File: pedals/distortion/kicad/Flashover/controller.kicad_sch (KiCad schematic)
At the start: 24 parts, among them J4 SWD, U4 RP2040, U5 W25Q16JVSS, U6 AP2112K-3.3, Y1 12MHz

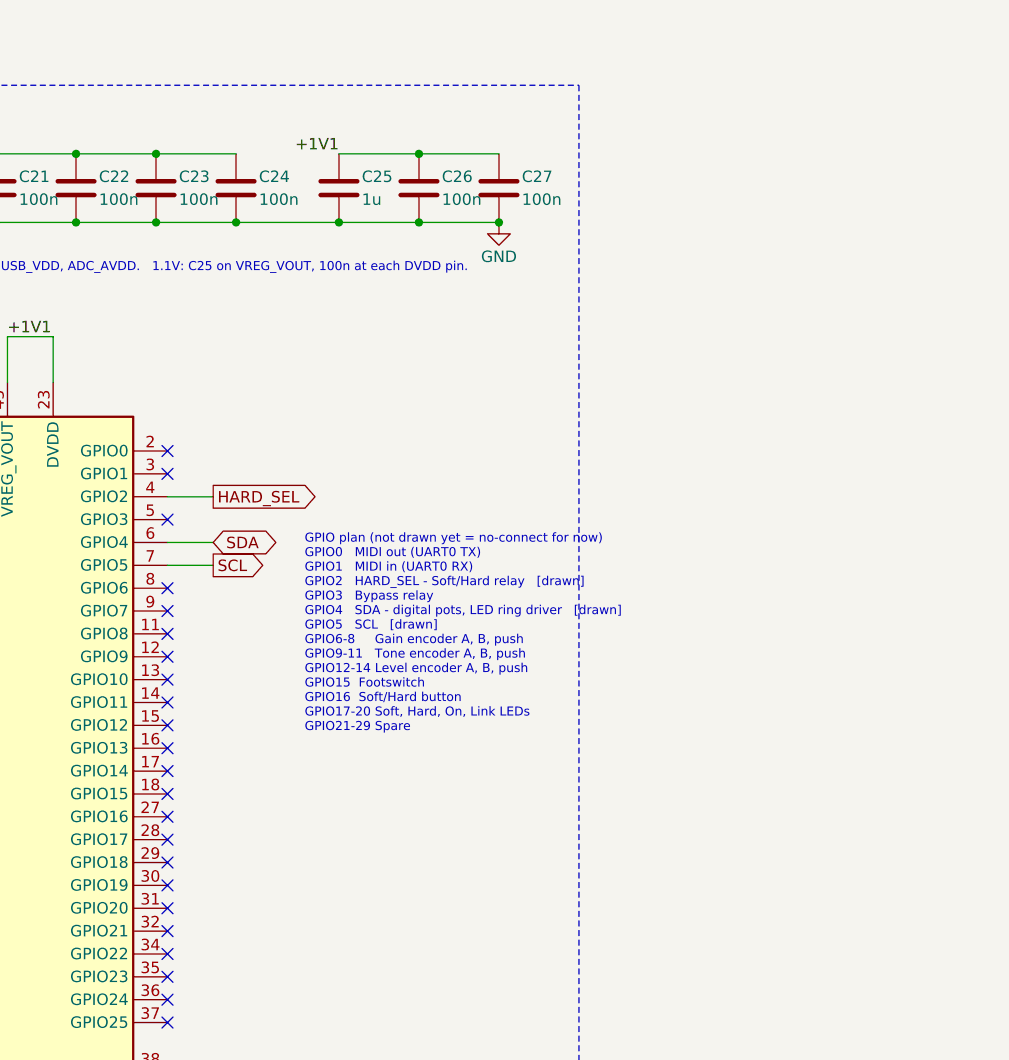
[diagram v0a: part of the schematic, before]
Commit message: Add Flashover controls and LED ring sheets
Controls sheet: three PEC11R encoders with push switches (pull-ups and
RC filtering) and the Soft/Hard button. LED Rings sheet: IS31FL3236A
driving three 11-LED rings plus Soft, Hard and On LEDs, on its own I2C
bus. Controller sheet wires the new GPIOs; the 5V regulator becomes an
L7805 for the LED load. ERC clean.

Co-Authored-By: Claude Opus 5.5 <noreply@anthropic.com>
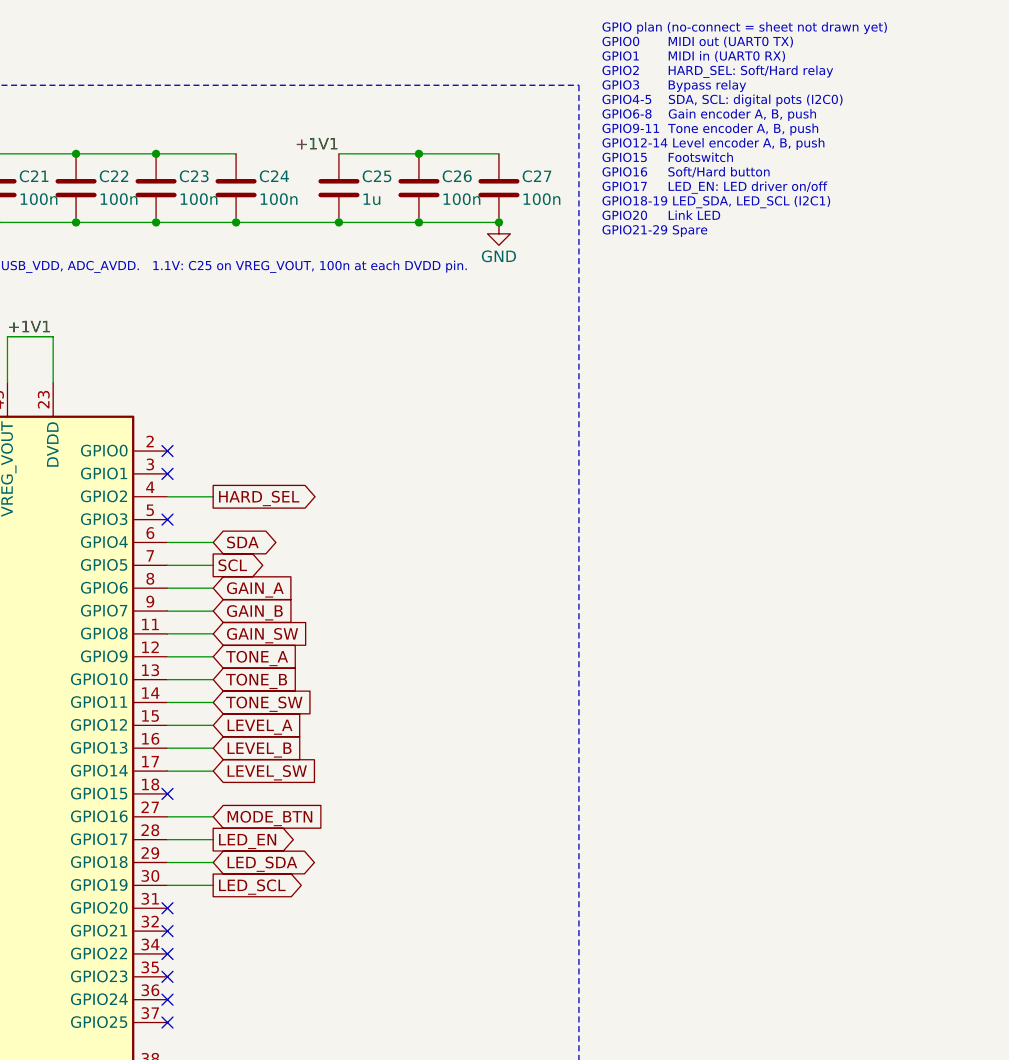
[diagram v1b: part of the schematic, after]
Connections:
- net GAIN_SW: now reaches U4.11 (GPIO8)
- net TONE_A: now reaches U4.12 (GPIO9)
- net TONE_B: now reaches U4.13 (GPIO10)
- net TONE_SW: now reaches U4.14 (GPIO11)
- net LEVEL_A: now reaches U4.15 (GPIO12)
- net LEVEL_B: now reaches U4.16 (GPIO13)
- net LEVEL_SW: now reaches U4.17 (GPIO14)
- net MODE_BTN: now reaches U4.27 (GPIO16)
- net LED_EN: now reaches U4.28 (GPIO17)
- net LED_SDA: now reaches U4.29 (GPIO18)
- net LED_SCL: now reaches U4.30 (GPIO19)
- net GAIN_A: now reaches U4.8 (GPIO6)
- net GAIN_B: now reaches U4.9 (GPIO7)
- no-connect marks 30 -> 17
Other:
- note added: "GPIO plan (no-connect = sheet not drawn yet) GPIO0 MIDI out (UART0 TX) GPIO1 MIDI in (UART0 RX) GPIO2 HARD_SEL: Soft/Hard relay GPIO3 Bypass relay GPIO4-5 SDA, SCL: digital pots (I2C0) GPIO6-8 Gain encoder A, B, push GPIO9-11 Tone encoder A, B, push GPIO12-14 Level encoder A, B, push GPIO15 Footswitch GPIO16 Soft/Hard button GPIO17 LED_EN: LED driver on/off GPIO18-19 LED_SDA, LED_SCL (I2C1) GPIO2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"
- note removed: "GPIO plan (not drawn yet = no-connect for now) GPIO0 MIDI out (UART0 TX) GPIO1 MIDI in (UART0 RX) GPIO2 HARD_SEL - Soft/Hard relay [drawn] GPIO3 Bypass relay GPIO4 SDA - digital pots, LED ring driver [drawn] GPIO5 SCL [drawn] GPIO6-8 Gain encoder A, B, push GPIO9-11 Tone encoder A, B, push GPIO12-14 Level encoder A, B, push GPIO15 Footswitch GPIO16 Soft/Hard button GPIO17-20 Soft, Hard, On, Link 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"

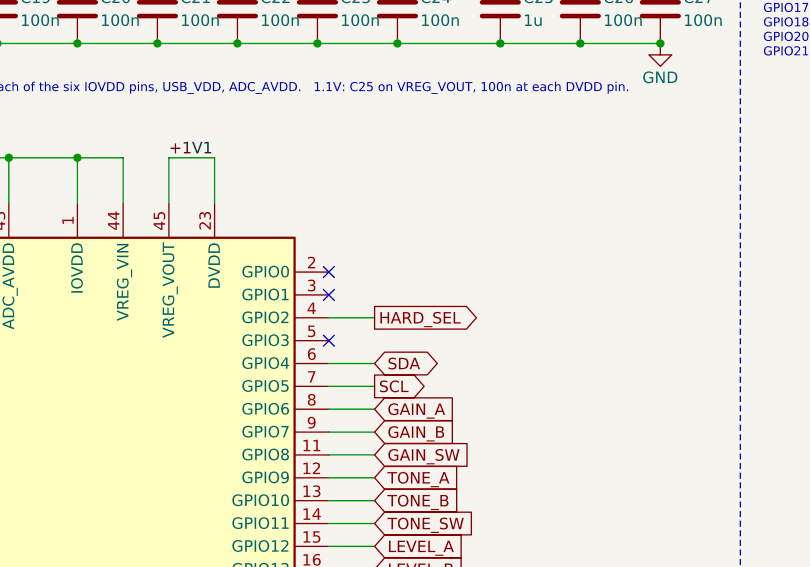
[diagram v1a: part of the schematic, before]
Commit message: Add Flashover MIDI sheet
MIDI in (H11L1 optocoupler, 220 ohm, reverse-protection diode, sleeve
unconnected) and MIDI out (3.3V drive: 33 ohm to pin 4, 10 ohm to pin 5)
on 3.5 mm TRS Type A jacks, wired to UART0. Root sheet re-spaced for
nine sheets. ERC clean.

Co-Authored-By: Claude Opus 5.5 <noreply@anthropic.com>
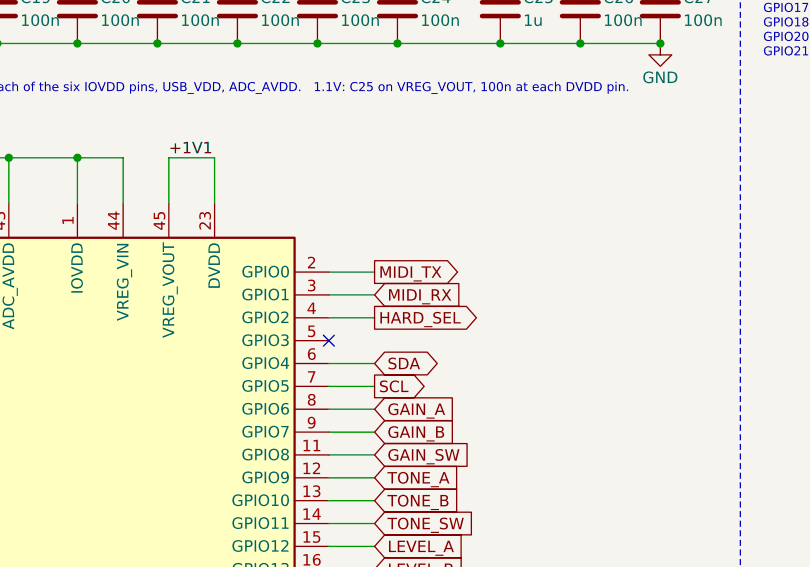
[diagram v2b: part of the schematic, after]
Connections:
- net MIDI_TX: now reaches U4.2 (GPIO0)
- net MIDI_RX: now reaches U4.3 (GPIO1)
- no-connect marks 17 -> 15

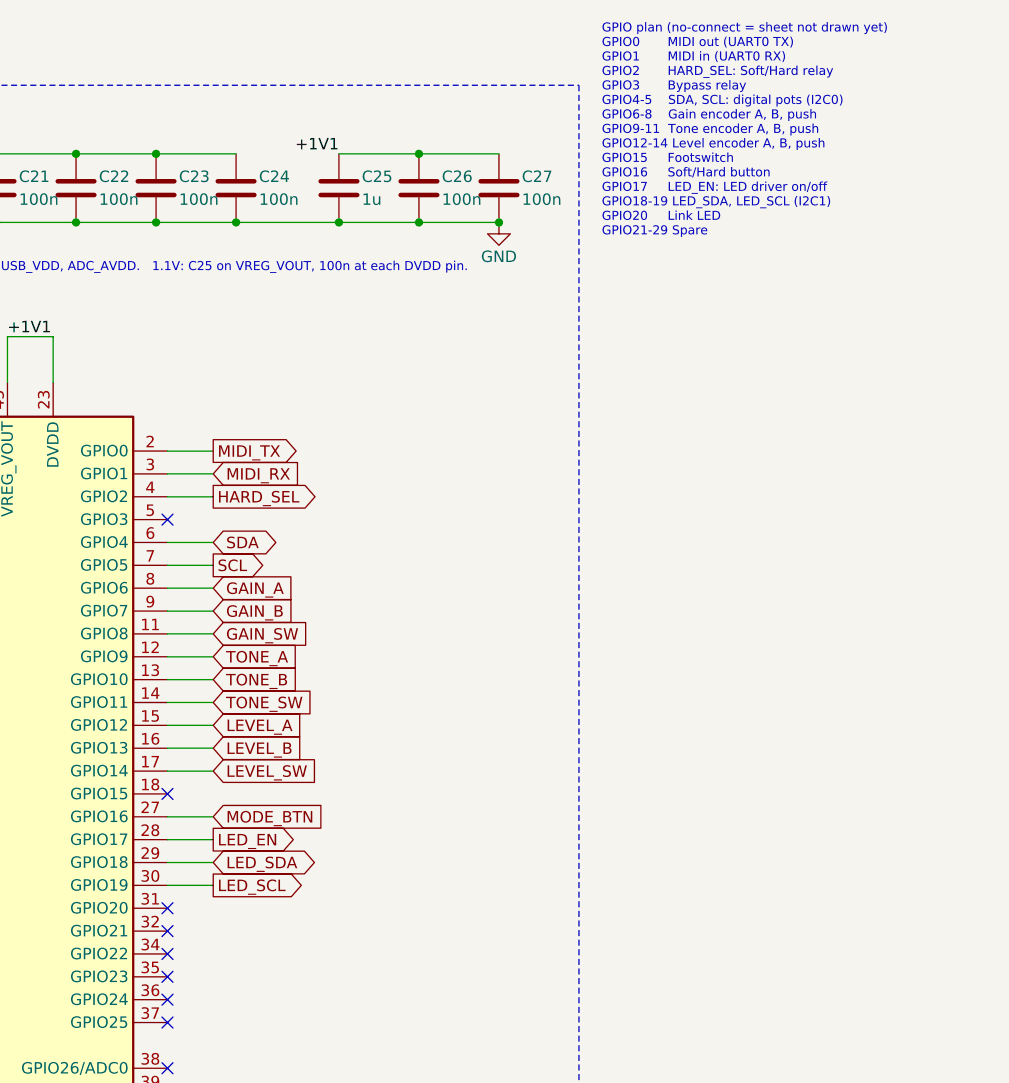
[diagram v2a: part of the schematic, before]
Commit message: Add Flashover bypass sheet; complete schematic
Bypass sheet: fail-safe G6K-2 relay bypass (NC contacts join the jacks
when unpowered), input/output jacks moved here from the audio sheets
(now FX_IN/FX_OUT), relay driver on FX_ON, soft-touch footswitch and
Link LED. Relay coils on K1 and K2 now take +5V on pin 1 (marked +).
Root sheet laid out in four columns. ERC clean.

Co-Authored-By: Claude Opus 5.5 <noreply@anthropic.com>
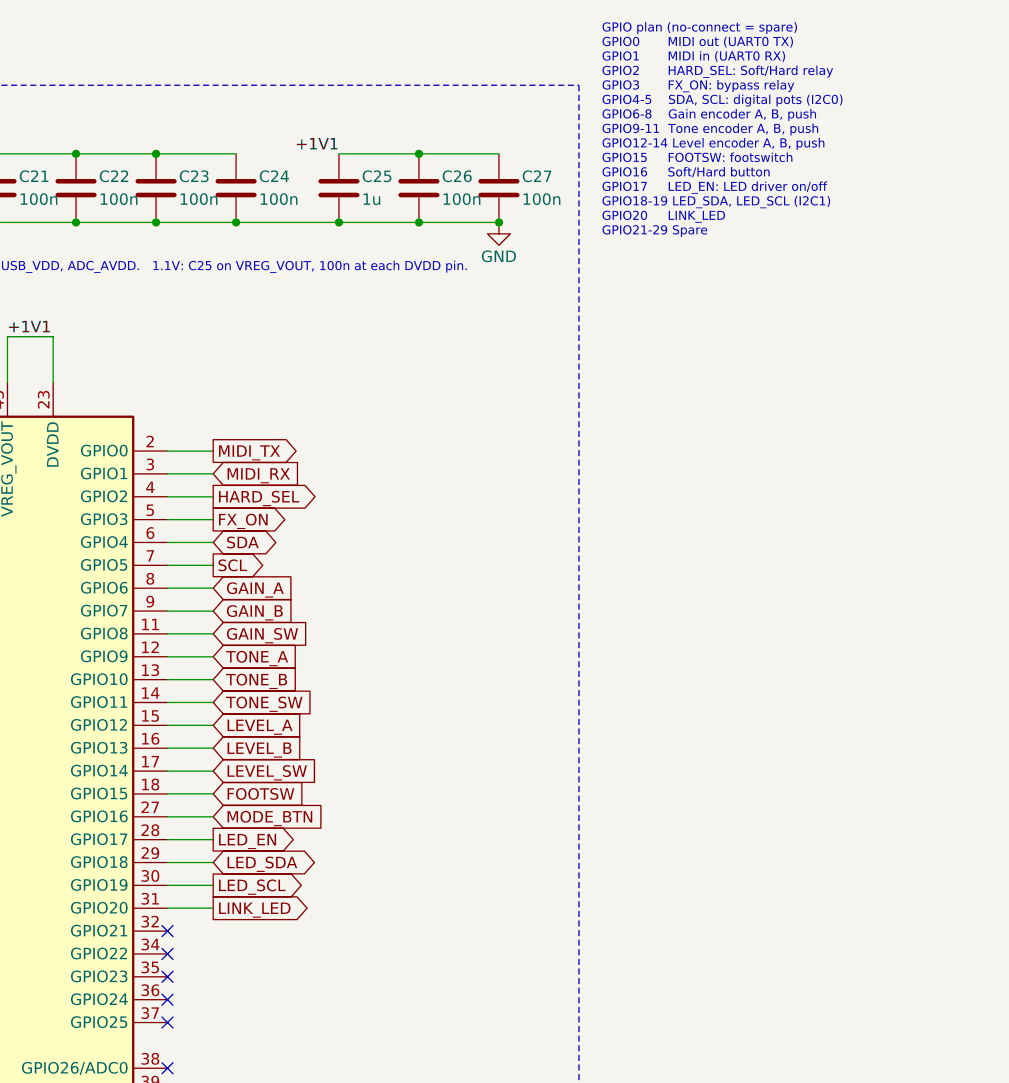
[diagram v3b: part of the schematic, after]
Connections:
- net FOOTSW: now reaches U4.18 (GPIO15)
- net LINK_LED: now reaches U4.31 (GPIO20)
- net FX_ON: now reaches U4.5 (GPIO3)
- no-connect marks 15 -> 12
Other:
- note added: "GPIO plan (no-connect = spare) GPIO0 MIDI out (UART0 TX) GPIO1 MIDI in (UART0 RX) GPIO2 HARD_SEL: Soft/Hard relay GPIO3 FX_ON: bypass relay GPIO4-5 SDA, SCL: digital pots (I2C0) GPIO6-8 Gain encoder A, B, push GPIO9-11 Tone encoder A, B, push GPIO12-14 Level encoder A, B, push GPIO15 FOOTSW: footswitch GPIO16 Soft/Hard button GPIO17 LED_EN: LED driver on/off GPIO18-19 LED_SDA, LED_SCL (I2C1) GPIO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"
- note removed: "GPIO plan (no-connect = sheet not drawn yet) GPIO0 MIDI out (UART0 TX) GPIO1 MIDI in (UART0 RX) GPIO2 HARD_SEL: Soft/Hard relay GPIO3 Bypass relay GPIO4-5 SDA, SCL: digital pots (I2C0) GPIO6-8 Gain encoder A, B, push GPIO9-11 Tone encoder A, B, push GPIO12-14 Level encoder A, B, push GPIO15 Footswitch GPIO16 Soft/Hard button GPIO17 LED_EN: LED driver on/off GPIO18-19 LED_SDA, LED_SCL (I2C1) GPIO2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"

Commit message: Assign Flashover footprints
Surface-mount for assembly; through-hole for jacks, encoders, panel LEDs,
the Soft/Hard button, the TO-220 regulator and the germanium diodes.
Q1/Q2 use the MMBT3904 symbol, 1N4148 -> 1N4148W, 1N5817 -> SS14.

Co-Authored-By: Claude Opus 5.5 <noreply@anthropic.com>
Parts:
- C16, C17, C18, C19, C20, C21, C22, C23, C24, C25, C26, C27, C28, C29, C30, C31, C32: footprint (none) -> Capacitor_SMD:C_0805_2012Metric
- J4: footprint (none) -> Connector_JST:JST_SH_SM03B-SRSS-TB_1x03-1MP_P1.00mm_Horizontal
- R19, R20: footprint (none) -> Resistor_SMD:R_0805_2012Metric
- U4: footprint (none) -> Package_DFN_QFN:QFN-56-1EP_7x7mm_P0.4mm_EP3.2x3.2mm
- U5: footprint (none) -> Package_SO:SOIC-8_5.3x5.3mm_P1.27mm
- U6: footprint (none) -> Package_TO_SOT_SMD:SOT-23-5
- Y1: footprint (none) -> Crystal:Crystal_SMD_3225-4Pin_3.2x2.5mm
